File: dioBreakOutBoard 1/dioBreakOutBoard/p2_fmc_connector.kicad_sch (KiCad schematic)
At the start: 9 parts, among them J1 Conn_01x03_Pin, P1 Samtec_ASP-134606-01

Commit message: C:\Users\khernandez\KiCad\KiCad-Projects# Please enter the commit message for your changes. Lines starting
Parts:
- removed D1, D3: GRN LED, LED_SMD:LED_0603_1608Metric, symbol Device:LED
- removed J1: Conn_01x03_Pin, Connector_TE-Connectivity:TE_826576-3_1x03_P3.96mm_Vertical, symbol Connector:Conn_01x03_Pin
- removed R2, R3: 1k, Resistor_SMD:R_0603_1608Metric_Pad0.98x0.95mm_HandSolder, symbol Device:R_US
- removed TP3: TestPoint, PB:TP_5011series, symbol Connector:TestPoint
- D2: footprint PB:LED_WP934CB&slash_GD_KNB -> LED_SMD:LED_0603_1608Metric_Pad1.05x0.95mm_HandSolder; MFG_PN WP934CB/GD -> SML-E12P8WT86
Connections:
- net +3.3VA is gone; now on net +3V3: P1.D32 (Pin_32)
- net FMC1_DP0.P is gone; now on net GND: P1.C2 (Pin_2), P1.C6 (Pin_6)
- net FMC1_DP0.N renamed +1V8
- net VDD renamed VADJ
- no-connect marks 10 -> 16
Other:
- note removed: "-12V"
- note removed: "12V"
- note removed: "GBT LOOP BACKS"

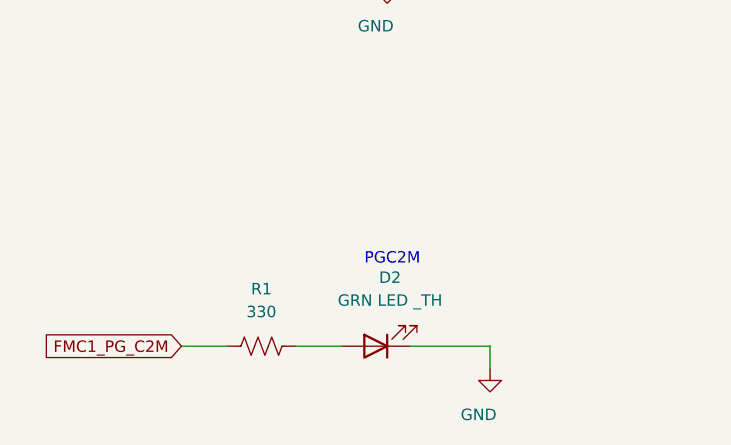
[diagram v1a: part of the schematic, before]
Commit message: added 2 bit buffers, which replace the previous 8 bit buffers
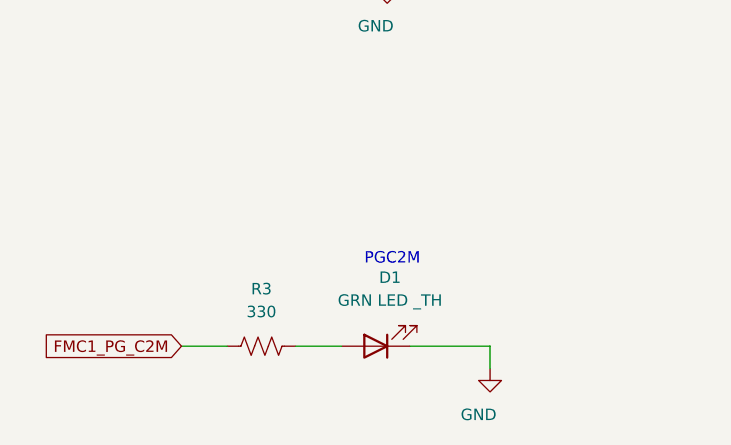
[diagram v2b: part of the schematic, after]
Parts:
- renumbered D2 to D1, R1 to R3
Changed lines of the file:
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@@
 (kicad_sch
-	(version 20231120)
+	(version 20250114)
 	(generator "eeschema")
-	(generator_version "8.0")
+	(generator_version "9.0")
 	(paper "B")
+	(text "PGC2M"
+		(exclude_from_sim no)
+		(at 82.55 210.82 0)
+		(effects
+			(font
+				(size 1.27 1.27)
+			)
+			(justify left bottom)
+		)
+	)
 	(junction
 		(at 85.09 139.7)
@@
 		)
 	)
-	(text "PGC2M"
-		(exclude_from_sim no)
-		(at 82.55 210.82 0)
-		(effects
-			(font
-				(size 1.27 1.27)
-			)
-			(justify left bottom)
-		)
-	)
 	(label "VADJ"
 		(at 342.9 177.8 0)
-		(fields_autoplaced yes)
 		(effects
 			(font
@@
 	(label "FMC1_GBTCLK0_M2C.P"
 		(at 149.86 85.09 0)
-		(fields_autoplaced yes)
 		(effects
 			(font
@@
 	(label "PRSNT_M2C_L"
 		(at 334.01 81.28 0)
-		(fields_autoplaced yes)
 		(effects
 			(font
@@
 	(label "FMC1_DP0_M2C.N"
 		(at 67.31 93.98 0)
-		(fields_autoplaced yes)
 		(effects
 			(font
@@
 	(label "FMC1_DP0_M2C.P"
 		(at 67.31 91.44 0)
-		(fields_autoplaced yes)
 		(effects
 			(font
@@
 	(label "FMC1_CLK0_M2C.N"
 		(at 330.2 88.9 0)
-		(fields_autoplaced yes)
 		(effects
 			(font
@@
 	(label "TDI"
 		(at 169.926 151.13 0)
-		(fields_autoplaced yes)
 		(effects
 			(font
@@
 	(label "FMC1_DP0_C2M.N"
 		(at 67.31 83.82 0)
-		(fields_autoplaced yes)
 		(effects
 			(font
@@
 	(label "FMC1_GBTCLK0_M2C.N"
 		(at 149.86 87.63 0)
-		(fields_autoplaced yes)
 		(effects
 			(font
@@
 	(label "FMC1_DP0_C2M.P"
 		(at 67.31 81.28 0)
-		(fields_autoplaced yes)
 		(effects
 			(font
@@
 	(label "TMS"
 		(at 169.672 158.75 0)
-		(fields_autoplaced yes)
 		(effects
 			(font
@@
 	(label "VADJ"
 		(at 266.7 177.8 0)
-		(fields_autoplaced yes)
 		(effects
 			(font
@@
 	(label "FMC1_CLK0_M2C.P"
 		(at 330.2 86.36 0)
-		(fields_autoplaced yes)
 		(effects
 			(font
@@
 	(label "VREF_A_M2C"
 		(at 334.01 78.74 0)
-		(fields_autoplaced yes)
 		(effects
 			(font
@@
 		)
 	)
+	(global_label "FMC1_LA23.N"
+		(shape bidirectional)
+		(at 163.83 135.89 180)
+		(fields_autoplaced yes)
+		(effects
+			(font
+				(size 1.27 1.27)
+			)
+			(justify right)
+		)
+		(property "Intersheetrefs" "${INTERSHEET_REFS}"
+			(at 147.2754 135.89 0)
+			(effects
+				(font
+					(size 1.27 1.27)
+				)
+				(justify right)
+				(hide yes)
+			)
+		)
+	)
 	(global_label "FMC1_LA15.P"
 		(shape bidirectional)
@@
 		)
 	)
+	(global_label "FMC1_LA23.P"
+		(shape bidirectional)
+		(at 163.83 133.35 180)
+		(fields_autoplaced yes)
+		(effects
+			(font
+				(size 1.27 1.27)
+			)
+			(justify right)
+		)
+		(property "Intersheetrefs" "${INTERSHEET_REFS}"
+			(at 147.3359 133.35 0)
+			(effects
+				(font
+					(size 1.27 1.27)
+				)
+				(justify right)
+				(hide yes)
+			)
+		)
+	)
 	(global_label "FMC1_LA17_CC.P"
 		(shape bidirectional)
@@
 		)
 	)
-	(global_label "FMC1_LA23.N"
-		(shape bidirectional)
-		(at 163.83 135.89 180)
-		(fields_autoplaced yes)
-		(effects
-			(font
-				(size 1.27 1.27)
-			)
-			(justify right)
-		)
-		(property "Intersheetrefs" "${INTERSHEET_REFS}"
-			(at 147.2754 135.89 0)
-			(effects
-				(font
-					(size 1.27 1.27)
-				)
-				(justify right)
-				(hide yes)
-			)
-		)
-	)
 	(global_label "FMC1_LA31.N"
 		(shape bidirectional)
@@
 		)
 	)
-	(global_label "FMC1_LA23.P"
-		(shape bidirectional)
-		(at 163.83 133.35 180)
-		(fields_autoplaced yes)
-		(effects
-			(font
-				(size 1.27 1.27)
-			)
-			(justify right)
-		)
-		(property "Intersheetrefs" "${INTERSHEET_REFS}"
-			(at 147.3359 133.35 0)
-			(effects
-				(font
-					(size 1.27 1.27)
-				)
-				(justify right)
-				(hide yes)
-			)
-		)
-	)
 	(global_label "FMC1_LA20.N"
 		(shape bidirectional)
@@
 		(dnp no)
 		(fields_autoplaced yes)
-		(property "Reference" "D2"
+		(property "Reference" "D1"
 			(at 85.4075 212.09 0)
 			(effects
@@
 			(project "dioBreakOutBoard"
 				(path "/98e3a74d-079b-42d2-b386-3e452c68576a/ca1ae1b7-e807-4e93-87f8-4f39e01d0df1"
-					(reference "D2")
+					(reference "D1")
 					(unit 1)
 				)
@@
 		(on_board yes)
 		(dnp no)
-		(property "Reference" "#PWR010"
+		(property "Reference" "#PWR035"
 			(at 96.52 228.6 0)
 			(effects
@@
 			(project "dioBreakOutBoard"
 				(path "/98e3a74d-079b-42d2-b386-3e452c68576a/ca1ae1b7-e807-4e93-87f8-4f39e01d0df1"
-					(reference "#PWR010")
+					(reference "#PWR035")
 					(unit 1)
 				)
@@
 		(on_board yes)
 		(dnp no)
-		(property "Reference" "#PWR024"
+		(property "Reference" "#PWR038"
 			(at 271.78 187.96 0)
 			(effects
@@
 			(project "dioBreakOutBoard"
 				(path "/98e3a74d-079b-42d2-b386-3e452c68576a/ca1ae1b7-e807-4e93-87f8-4f39e01d0df1"
-					(reference "#PWR024")
+					(reference "#PWR038")
 					(unit 1)
 				)
@@
 		(on_board yes)
 		(dnp no)
-		(property "Reference" "#PWR018"
+		(property "Reference" "#PWR037"
 			(at 173.99 184.15 0)
 			(effects
@@
 			(project "dioBreakOutBoard"
 				(path "/98e3a74d-079b-42d2-b386-3e452c68576a/ca1ae1b7-e807-4e93-87f8-4f39e01d0df1"
-					(reference "#PWR018")
+					(reference "#PWR037")
 					(unit 1)
 				)
@@
 		(on_board yes)
 		(dnp no)
-		(property "Reference" "#PWR026"
+		(property "Reference" "#PWR040"
 			(at 350.52 185.42 0)
 			(effects
@@
 			(project "dioBreakOutBoard"
 				(path "/98e3a74d-079b-42d2-b386-3e452c68576a/ca1ae1b7-e807-4e93-87f8-4f39e01d0df1"
-					(reference "#PWR026")
+					(reference "#PWR040")
 					(unit 1)
 				)
@@
 		(on_board yes)
 		(dnp no)
-		(property "Reference" "#PWR051"
+		(property "Reference" "#PWR031"
 			(at 59.69 100.33 0)
 			(effects
@@
 			(project "dioBreakOutBoard"
 				(path "/98e3a74d-079b-42d2-b386-3e452c68576a/ca1ae1b7-e807-4e93-87f8-4f39e01d0df1"
-					(reference "#PWR051")
+					(reference "#PWR031")
 					(unit 1)
 				)
@@
 		(dnp no)
 		(fields_autoplaced yes)
-		(property "Reference" "R1"
+		(property "Reference" "R3"
 			(at 71.12 213.36 90)
 			(effects
@@
 			(project "dioBreakOutBoard"
 				(path "/98e3a74d-079b-42d2-b386-3e452c68576a/ca1ae1b7-e807-4e93-87f8-4f39e01d0df1"
-					(reference "R1")
+					(reference "R3")
 					(unit 1)
 				)
@@
 		(on_board yes)
 		(dnp no)
-		(property "Reference" "#PWR011"
+		(property "Reference" "#PWR034"
 			(at 85.09 185.42 0)
 			(effects
@@
 			(project "dioBreakOutBoard"
 				(path "/98e3a74d-079b-42d2-b386-3e452c68576a/ca1ae1b7-e807-4e93-87f8-4f39e01d0df1"
-					(reference "#PWR011")
+					(reference "#PWR034")
 					(unit 1)
 				)
@@
 		(dnp no)
 		(fields_autoplaced yes)
-		(property "Reference" "#PWR052"
+		(property "Reference" "#PWR032"
 			(at 62.23 80.01 0)
 			(effects
@@
 			(project "dioBreakOutBoard"
 				(path "/98e3a74d-079b-42d2-b386-3e452c68576a/ca1ae1b7-e807-4e93-87f8-4f39e01d0df1"
-					(reference "#PWR052")
+					(reference "#PWR032")
 					(unit 1)
 				)
@@
 		(on_board yes)
 		(dnp no)
-		(property "Reference" "#PWR016"
+		(property "Reference" "#PWR036"
 			(at 143.51 156.21 0)
 			(effects
@@
 			(project "dioBreakOutBoard"
 				(path "/98e3a74d-079b-42d2-b386-3e452c68576a/ca1ae1b7-e807-4e93-87f8-4f39e01d0df1"
-					(reference "#PWR016")
+					(reference "#PWR036")
 					(unit 1)
 				)
@@
 		(on_board yes)
 		(dnp no)
-		(property "Reference" "#PWR08"
+		(property "Reference" "#PWR033"
 			(at 68.58 179.07 0)
 			(effects
@@
 			(project "dioBreakOutBoard"
 				(path "/98e3a74d-079b-42d2-b386-3e452c68576a/ca1ae1b7-e807-4e93-87f8-4f39e01d0df1"
-					(reference "#PWR08")
+					(reference "#PWR033")
 					(unit 1)
 				)
@@
 		(on_board yes)
 		(dnp no)
-		(property "Reference" "#PWR081"
+		(property "Reference" "#PWR039"
 			(at 311.15 91.44 0)
 			(effects
@@
 			(project "dioBreakOutBoard"
 				(path "/98e3a74d-079b-42d2-b386-3e452c68576a/ca1ae1b7-e807-4e93-87f8-4f39e01d0df1"
-					(reference "#PWR081")
+					(reference "#PWR039")
 					(unit 1)
 				)
